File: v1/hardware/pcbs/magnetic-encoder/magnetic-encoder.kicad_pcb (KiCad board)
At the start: 2 copper layers, 50 x 50 mm, 25 parts, among them J1 S8B-XH-A, J2 S2B-XH-A, J3 S3B-XH-A, U1 SN74LVC1G14DBV

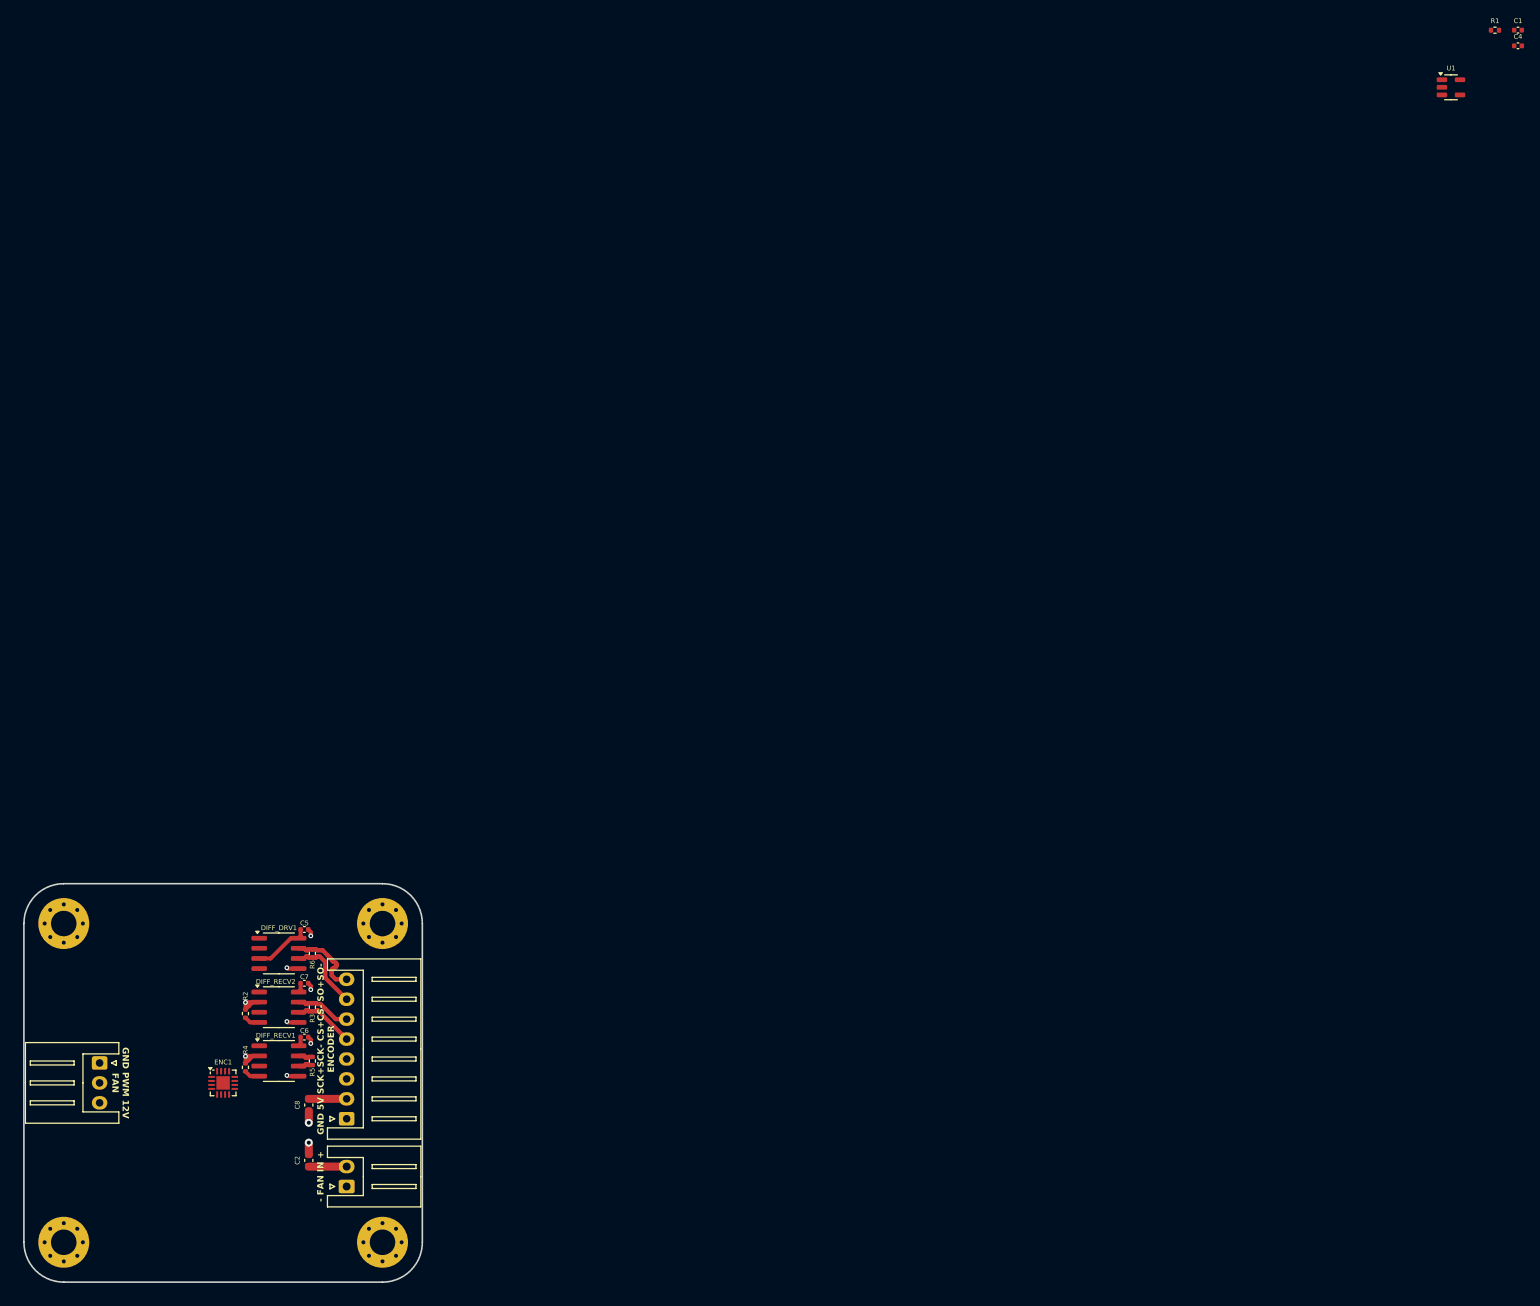
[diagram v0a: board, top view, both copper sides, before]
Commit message: magnetic encoder PCB done + production files
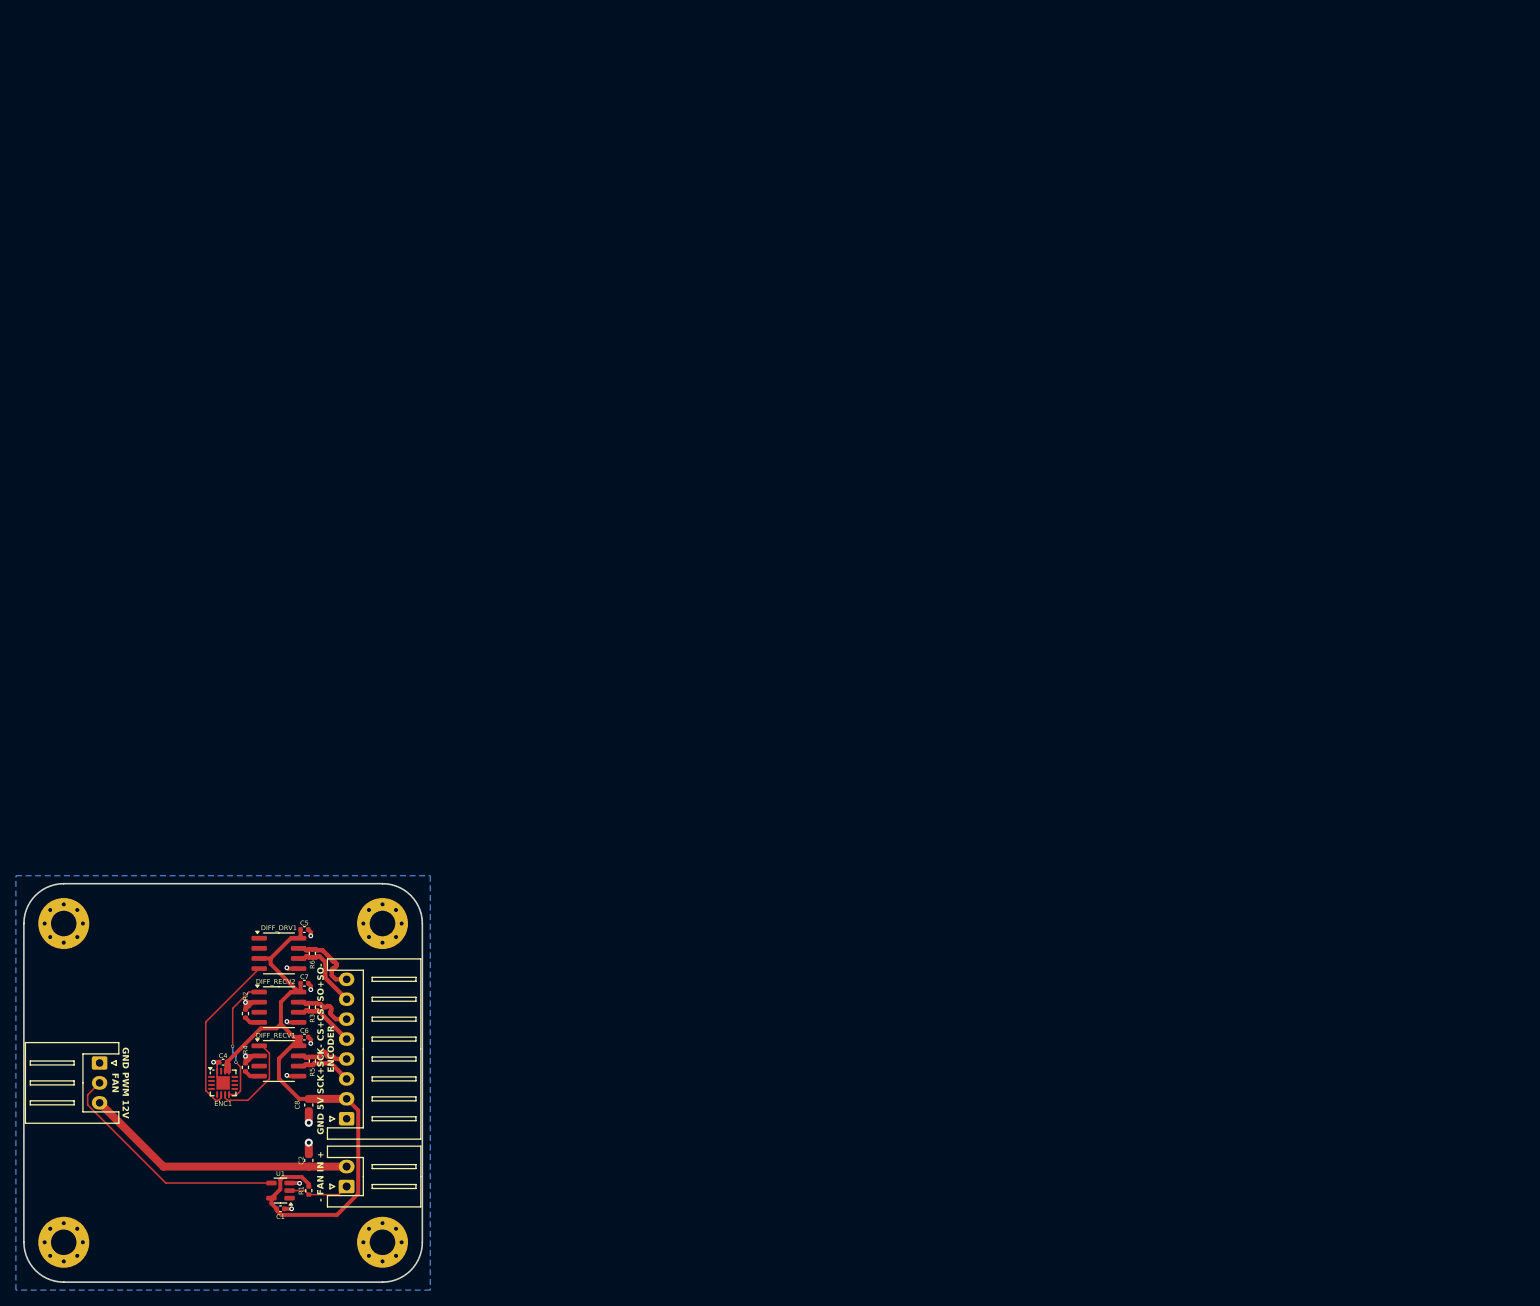
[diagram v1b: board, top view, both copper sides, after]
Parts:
- moved C1 214.5 mm to (7.20, 15.8), turned to 180 degrees
- moved R1 208.2 mm to (10.8, 13.5), turned to -90 degrees
- moved C4 206.6 mm to (0.00, -2.60)
- moved U1 201.8 mm to (7.20, 13.5), turned to 180 degrees
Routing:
- net +5V: track 14.3 -> 86.4 mm
- net /FAN_PWM: track 0.00 -> 30.5 mm
- net +12V: track 4.75 -> 34.3 mm
- net /ENC.MISO: track 0.00 -> 21.1 mm
- net /ENC.SCS: track 0.00 -> 16.6 mm, vias 0 -> 2
- net /ENC.SCLK: track 0.00 -> 12.1 mm
- net /FAN_PWM_INV: track 0.00 -> 7.80 mm
- net GND: track 21.0 -> 26.9 mm, vias 10 -> 13
- net /ENC_DIFF.SCLK+: track 1.87 -> 7.07 mm
- net /ENC_DIFF.SCLK-: track 1.87 -> 7.01 mm
- net /ENC_DIFF.SCS-: track 7.00 -> 7.66 mm
- added copper zone on B.Cu, net GND
